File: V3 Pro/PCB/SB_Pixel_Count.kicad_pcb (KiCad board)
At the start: 2 copper layers, 53.5 x 26.5 mm, 20 parts, among them J2 String1, J3 OLED, SW1 Test, SW2 Test, U1 74AHCT1G125, U2 MOUDLE-SEEEDUINO-XIAO, U3 AMS1117-5.0, U4 INA219BxD, U5 TF-123-ARP9H17

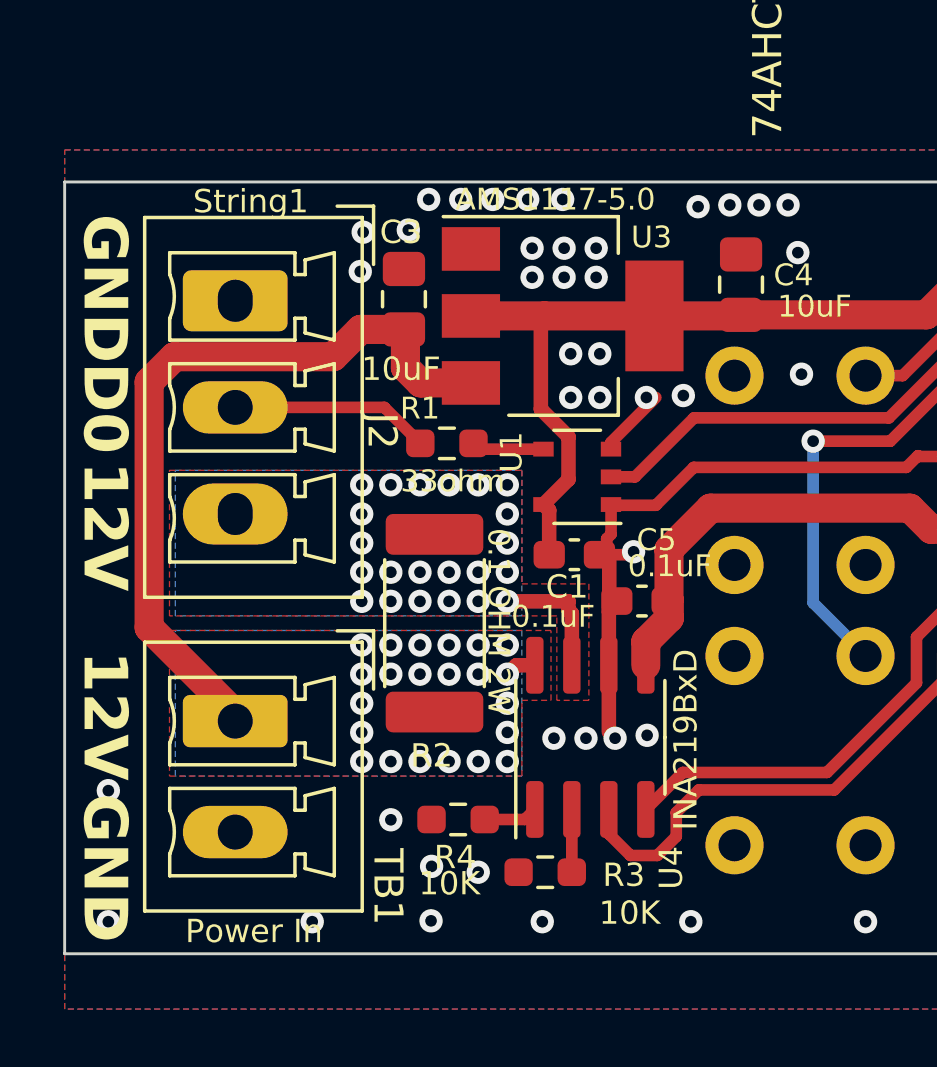
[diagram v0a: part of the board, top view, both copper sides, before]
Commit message: Add company name to title blocks; fix V3 Pro SW1/SW2 push-button DRC
Add (company "S&B Designs LLC") to V1/V2/V3 Pro's PCB and schematic
title blocks, matching V2 Lite, and add \${COMPANY} to each board's
silkscreen gr_text so it's printed on the physical board too.

Also includes KiCad-side board edits made while investigating the
SW1/SW2 "unconnected pad" DRC warnings on V3 Pro: added
lib/Scotts.pretty/SW_PUSH_6mm.kicad_mod, a copy of the standard
4-leg tactile switch footprint with unique pad numbers (1-4) instead
of the original's duplicated 1/1/2/2 numbering. The two redundant
mechanical-only legs (pads 3/4) are left with no net assigned, so
DRC's missing-connection check no longer applies to them. V3 Pro's
SW1/SW2 now use this footprint. Regenerated gerbers/BOM/fp-info-cache
reflect the resave.

Co-Authored-By: Claude Sonnet 5 <noreply@anthropic.com>
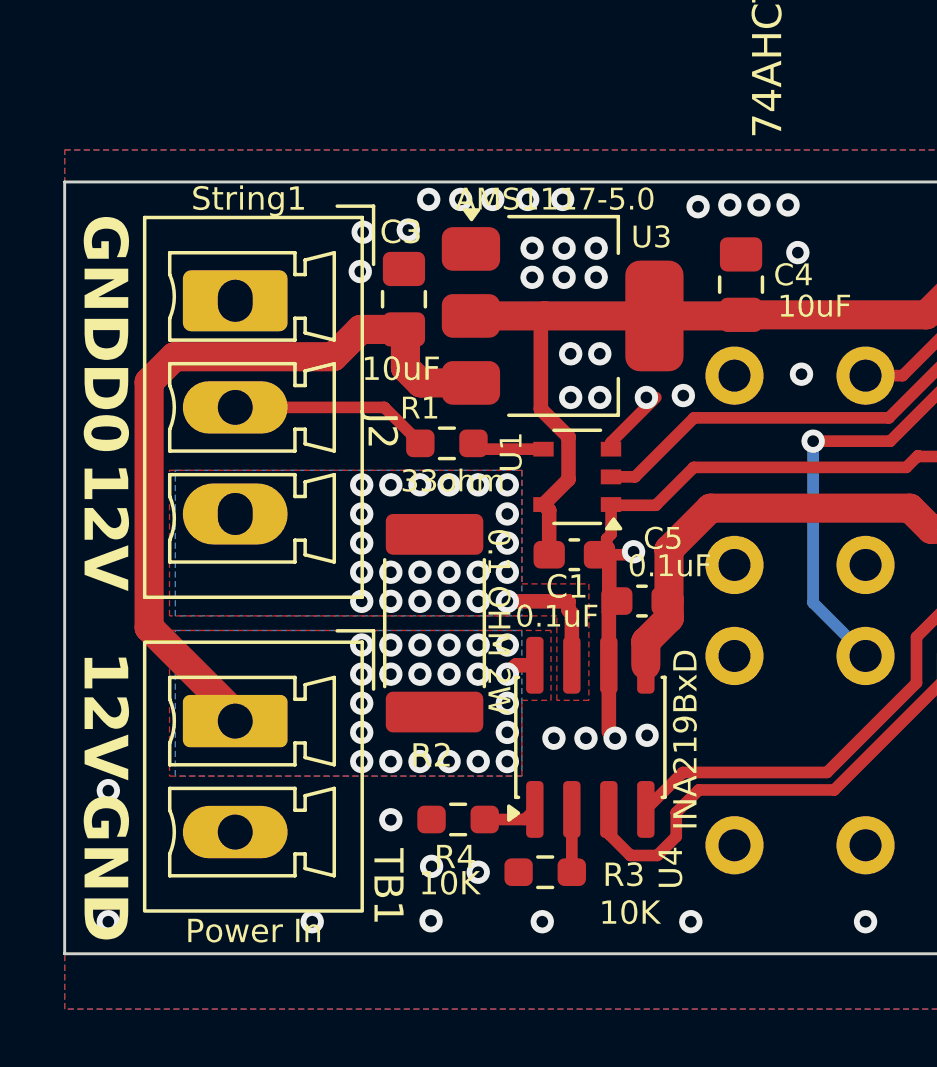
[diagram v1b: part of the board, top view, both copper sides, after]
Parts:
- SW1, SW2: footprint Button_Switch_THT:SW_PUSH_6mm -> Scotts:SW_PUSH_6mm
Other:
- board text added: "${TITLE} ${REVISION} ${COMPANY}"
- board text removed: "${TITLE} ${REVISION}"

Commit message: Add 4-pin SW_PUSH_6mm schematic symbol, wire pin 4 to GND
New lib/Scotts.kicad_sym symbol for the 4-leg tactile switch, split
into two units: unit 1 (pins 1/2) is the actual switch contact, unit
2 (pins 3/4) represents the redundant mechanical legs. Registered in
V3 Pro's sym-lib-table.

SW1/SW2 now place both units: pin 4 (the redundant GND-side leg) is
wired to GND for a second physical ground connection, pin 3 (the
redundant switch-side leg) is flagged no-connect and left genuinely
netless on the PCB, matching the earlier footprint fix. Includes the
regenerated gerbers/BOM/fp-info-cache from the KiCad resave.

Co-Authored-By: Claude Sonnet 5 <noreply@anthropic.com>
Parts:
- SW2: value Test -> Menu
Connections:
- SW1 pad 3: (no net) -> unconnected-(SW1-Pad3)
- SW1 pad 4: (no net) -> GND
- SW2 pad 3: (no net) -> unconnected-(SW2-Pad3)
- SW2 pad 4: (no net) -> GND
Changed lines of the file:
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@@
 	(net 22 "unconnected-(U5-SWITCH-Pad9)")
 	(net 23 "unconnected-(U5-DAT2-Pad1)")
+	(net 24 "unconnected-(SW1-Pad3)")
+	(net 25 "unconnected-(SW2-Pad3)")
 	(footprint "Resistor_SMD:R_2512_6332Metric_Pad1.40x3.35mm_HandSolder"
 		(layer "F.Cu")
@@
 		(tags "TF-SMD_TF-123-ARP9H15 footprint C2982548")
 		(property "Reference" "U5"
-			(at -0.000076 5.689916 90)
+			(at -0.000076 5.689916 270)
+			(unlocked yes)
 			(layer "B.SilkS")
 			(effects
@@
 		(property "Reference" "SW1"
 			(at 3.15 1.64 270)
+			(unlocked yes)
 			(layer "B.SilkS")
 			(effects
@@
 		)
 		(property "Value" "Test"
-			(at 3.75 -6.7 270)
-			(layer "B.Fab")
+			(at 3.07 -6.39 270)
+			(unlocked yes)
+			(layer "B.SilkS")
 			(effects
 				(font
@@
 			)
 		)
-		(property "Datasheet" ""
+		(property "Datasheet" "~"
 			(at 0 0 270)
 			(unlocked yes)
@@
 			)
 		)
-		(property "Description" ""
+		(property "Description" "Push button switch, 4-leg THT 6mm tactile. Legs 3/4 are redundant mechanical duplicates of legs 1/2 (same nets internally) - left as no-connect since the footprint leaves those pads netless."
 			(at 0 0 270)
 			(unlocked yes)
@@
 			(layers "*.Cu" "*.Mask")
 			(remove_unused_layers no)
+			(net 24 "unconnected-(SW1-Pad3)")
+			(pinfunction "3")
+			(pintype "passive+no_connect")
 		)
 		(pad "4" thru_hole circle
@@
 			(layers "*.Cu" "*.Mask")
 			(remove_unused_layers no)
+			(net 2 "GND")
+			(pinfunction "4")
+			(pintype "passive")
 		)
 		(embedded_fonts no)
@@
 		(property "Reference" "SW2"
 			(at 3.085 1.63 270)
+			(unlocked yes)
 			(layer "B.SilkS")
 			(effects
@@
 			)
 		)
-		(property "Value" "Test"
-			(at 3.75 -6.7 270)
-			(layer "B.Fab")
+		(property "Value" "Menu"
+			(at 3.255 -6.44 270)
+			(unlocked yes)
+			(layer "B.SilkS")
 			(effects
 				(font
@@
 			)
 		)
-		(property "Datasheet" ""
+		(property "Datasheet" "~"
 			(at 0 0 270)
 			(unlocked yes)
@@
 			)
 		)
-		(property "Description" ""
+		(property "Description" "Push button switch, 4-leg THT 6mm tactile. Legs 3/4 are redundant mechanical duplicates of legs 1/2 (same nets internally) - left as no-connect since the footprint leaves those pads netless."
 			(at 0 0 270)
 			(unlocked yes)
@@
 			(layers "*.Cu" "*.Mask")
 			(remove_unused_layers no)
+			(net 25 "unconnected-(SW2-Pad3)")
+			(pinfunction "3")
+			(pintype "passive+no_connect")
 		)
 		(pad "4" thru_hole circle
@@
 			(layers "*.Cu" "*.Mask")
 			(remove_unused_layers no)
+			(net 2 "GND")
+			(pinfunction "4")
+			(pintype "passive")
 		)
 		(embedded_fonts no)
@@
 	)
 	(gr_text "${TITLE} ${REVISION}\n${COMPANY}"
-		(at 117.55 92.67 270)
+		(at 116.41 87.51 270)
 		(layer "B.SilkS")
 		(effects
@@
 				(thickness 0.15)
 			)
-			(justify left bottom mirror)
+			(justify bottom mirror)
 		)
 	)
